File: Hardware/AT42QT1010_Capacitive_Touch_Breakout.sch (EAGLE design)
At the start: 28 parts, among them Q1 600mA/40V, U1 AT42QT1010 - UDFN

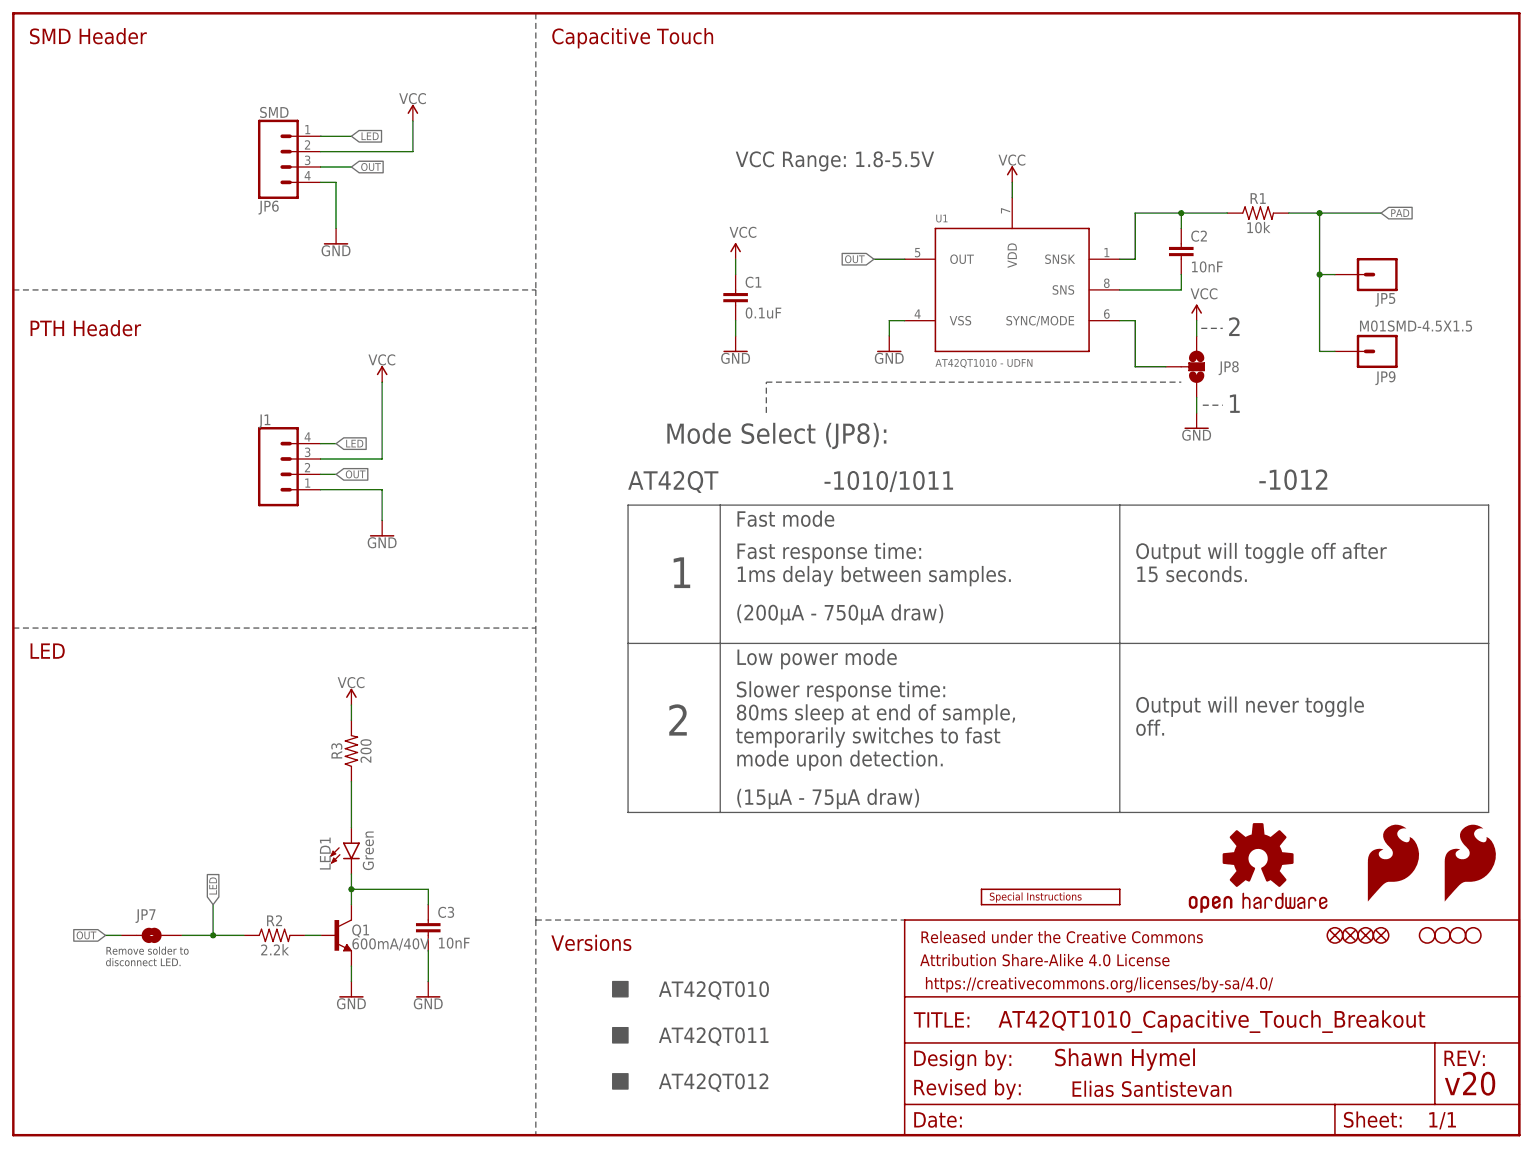
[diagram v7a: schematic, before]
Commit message: Update for REDS review
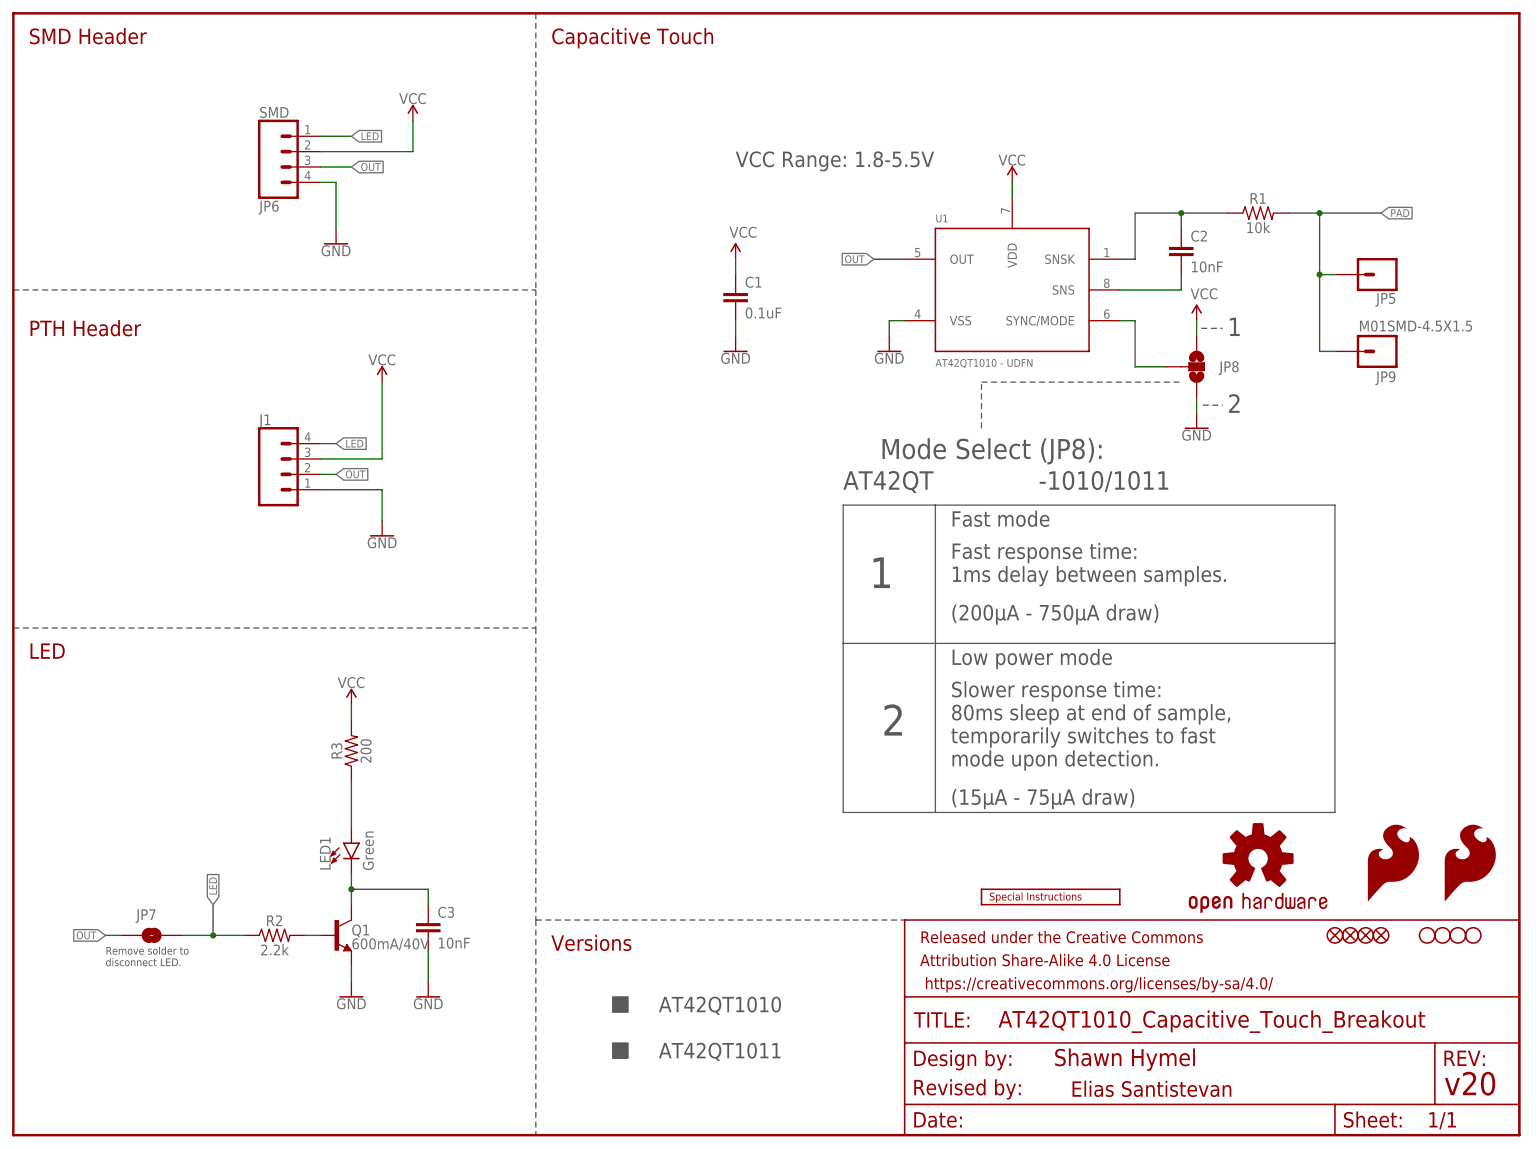
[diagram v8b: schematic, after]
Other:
- note added: "AT42QT1010"
- note added: "AT42QT1011"
- note removed: "-1012"
- note removed: "AT42QT010"
- note removed: "AT42QT011"
- note removed: "AT42QT012"
- note removed: "Output will never toggle off."
- note removed: "Output will toggle off after 15 seconds."
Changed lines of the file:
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@@
 <layer number="255" name="routoute" color="7" fill="1" visible="yes" active="yes"/>
 </layers>
-<schematic xreflabel="%F%N/%S" xrefpart="/%S.%C%R">
+<schematic xreflabel="%F%N/%S" xrefpart="1_/%S.%C%R">
 <attributes>
 </attributes>
@@
 <text x="2.54" y="132.08" size="2.54" layer="94" font="vector">PTH Header</text>
 <text x="2.54" y="78.74" size="2.54" layer="94" font="vector">LED</text>
-<text x="144.78" y="106.68" size="3.048" layer="97" font="vector" align="bottom-center">-1010/1011</text>
-<text x="119.38" y="100.584" size="2.54" layer="97" font="vector" ratio="15">Fast mode</text>
-<text x="119.38" y="91.44" size="2.54" layer="97" font="vector">Fast response time:
+<text x="180.34" y="106.68" size="3.048" layer="97" font="vector" align="bottom-center">-1010/1011</text>
+<text x="154.94" y="100.584" size="2.54" layer="97" font="vector" ratio="15">Fast mode</text>
+<text x="154.94" y="91.44" size="2.54" layer="97" font="vector">Fast response time:
 1ms delay between samples.</text>
-<text x="119.38" y="77.724" size="2.54" layer="97" font="vector" ratio="15">Low power mode</text>
-<text x="119.38" y="54.61" size="2.54" layer="97" font="vector">(15µA - 75µA draw)</text>
-<text x="119.38" y="60.96" size="2.54" layer="97" font="vector">Slower response time:
+<text x="154.94" y="77.724" size="2.54" layer="97" font="vector" ratio="15">Low power mode</text>
+<text x="154.94" y="54.61" size="2.54" layer="97" font="vector">(15µA - 75µA draw)</text>
+<text x="154.94" y="60.96" size="2.54" layer="97" font="vector">Slower response time:
 80ms sleep at end of sample,
 temporarily switches to fast
 mode upon detection.</text>
-<text x="119.38" y="85.09" size="2.54" layer="97" font="vector">(200µA - 750µA draw)</text>
-<wire x1="182.88" y1="104.14" x2="243.84" y2="104.14" width="0.1524" layer="97"/>
-<wire x1="243.84" y1="104.14" x2="243.84" y2="81.28" width="0.1524" layer="97"/>
-<wire x1="243.84" y1="81.28" x2="243.84" y2="53.34" width="0.1524" layer="97"/>
-<wire x1="243.84" y1="53.34" x2="182.88" y2="53.34" width="0.1524" layer="97"/>
+<text x="154.94" y="85.09" size="2.54" layer="97" font="vector">(200µA - 750µA draw)</text>
 <text x="148.59" y="6.604" size="2.54" layer="94" font="vector">Revised by:</text>
 <text x="174.752" y="6.35" size="2.54" layer="94" font="vector" ratio="10">Elias Santistevan</text>
@@
 <text x="15.24" y="27.94" size="1.27" layer="97" font="vector">Remove solder to
 disconnect LED.</text>
-<text x="126.238" y="114.3" size="3.302" layer="97" font="vector" ratio="10" align="bottom-center">Mode Select (JP8):</text>
-<wire x1="101.6" y1="104.14" x2="116.84" y2="104.14" width="0.1524" layer="97"/>
-<wire x1="116.84" y1="104.14" x2="182.88" y2="104.14" width="0.1524" layer="97"/>
-<wire x1="182.88" y1="104.14" x2="182.88" y2="81.28" width="0.1524" layer="97"/>
-<wire x1="182.88" y1="81.28" x2="182.88" y2="53.34" width="0.1524" layer="97"/>
-<wire x1="182.88" y1="53.34" x2="116.84" y2="53.34" width="0.1524" layer="97"/>
-<wire x1="116.84" y1="53.34" x2="101.6" y2="53.34" width="0.1524" layer="97"/>
-<wire x1="101.6" y1="53.34" x2="101.6" y2="81.28" width="0.1524" layer="97"/>
-<wire x1="101.6" y1="81.28" x2="101.6" y2="104.14" width="0.1524" layer="97"/>
-<wire x1="101.6" y1="81.28" x2="182.88" y2="81.28" width="0.1524" layer="97"/>
-<wire x1="116.84" y1="104.14" x2="116.84" y2="53.34" width="0.1524" layer="97"/>
-<text x="185.42" y="91.44" size="2.54" layer="97" font="vector">Output will toggle off after
-15 seconds.</text>
-<text x="185.42" y="66.04" size="2.54" layer="97" font="vector">Output will never toggle
-off.</text>
-<wire x1="182.88" y1="81.28" x2="243.84" y2="81.28" width="0.2032" layer="97"/>
-<text x="108.458" y="90.424" size="5.08" layer="97" font="vector" ratio="15">1</text>
-<text x="107.95" y="66.04" size="5.08" layer="97" font="vector" ratio="15">2</text>
-<text x="205.74" y="106.68" size="3.302" layer="97" font="vector">-1012</text>
-<wire x1="124.46" y1="119.38" x2="124.46" y2="124.46" width="0.2032" layer="97" style="shortdash"/>
-<wire x1="124.46" y1="124.46" x2="193.04" y2="124.46" width="0.2032" layer="97" style="shortdash"/>
-<text x="101.6" y="106.68" size="3.048" layer="97" font="vector">AT42QT </text>
+<text x="161.798" y="111.76" size="3.302" layer="97" font="vector" ratio="10" align="bottom-center">Mode Select (JP8):</text>
+<wire x1="137.16" y1="104.14" x2="152.4" y2="104.14" width="0.1524" layer="97"/>
+<wire x1="152.4" y1="104.14" x2="218.44" y2="104.14" width="0.1524" layer="97"/>
+<wire x1="218.44" y1="104.14" x2="218.44" y2="81.28" width="0.1524" layer="97"/>
+<wire x1="218.44" y1="81.28" x2="218.44" y2="53.34" width="0.1524" layer="97"/>
+<wire x1="218.44" y1="53.34" x2="152.4" y2="53.34" width="0.1524" layer="97"/>
+<wire x1="152.4" y1="53.34" x2="137.16" y2="53.34" width="0.1524" layer="97"/>
+<wire x1="137.16" y1="53.34" x2="137.16" y2="81.28" width="0.1524" layer="97"/>
+<wire x1="137.16" y1="81.28" x2="137.16" y2="104.14" width="0.1524" layer="97"/>
+<wire x1="137.16" y1="81.28" x2="218.44" y2="81.28" width="0.1524" layer="97"/>
+<wire x1="152.4" y1="104.14" x2="152.4" y2="53.34" width="0.1524" layer="97"/>
+<text x="141.478" y="90.424" size="5.08" layer="97" font="vector" ratio="15">1</text>
+<text x="143.51" y="66.04" size="5.08" layer="97" font="vector" ratio="15">2</text>
+<wire x1="160.02" y1="116.84" x2="160.02" y2="124.46" width="0.2032" layer="97" style="shortdash"/>
+<wire x1="160.02" y1="124.46" x2="193.04" y2="124.46" width="0.2032" layer="97" style="shortdash"/>
+<text x="137.16" y="106.68" size="3.048" layer="97" font="vector">AT42QT </text>
 <wire x1="86.36" y1="35.56" x2="147.32" y2="35.56" width="0.2032" layer="97" style="shortdash"/>
 <text x="88.9" y="30.48" size="2.54" layer="94" font="vector">Versions</text>
-<text x="106.68" y="22.86" size="2.54" layer="97" font="vector">AT42QT010</text>
-<text x="106.68" y="15.24" size="2.54" layer="97" font="vector">AT42QT011</text>
-<text x="106.68" y="7.62" size="2.54" layer="97" font="vector">AT42QT012</text>
+<text x="106.68" y="20.32" size="2.54" layer="97" font="vector">AT42QT1010</text>
+<text x="106.68" y="12.7" size="2.54" layer="97" font="vector">AT42QT1011</text>
 <polygon width="0.2032" layer="97">
-<vertex x="99.06" y="25.4"/>
 <vertex x="99.06" y="22.86"/>
+<vertex x="99.06" y="20.32"/>
+<vertex x="101.6" y="20.32"/>
 <vertex x="101.6" y="22.86"/>
-<vertex x="101.6" y="25.4"/>
 </polygon>
 <polygon width="0.2032" layer="97">
-<vertex x="99.06" y="17.78"/>
 <vertex x="99.06" y="15.24"/>
+<vertex x="99.06" y="12.7"/>
+<vertex x="101.6" y="12.7"/>
 <vertex x="101.6" y="15.24"/>
-<vertex x="101.6" y="17.78"/>
 </polygon>
-<polygon width="0.2032" layer="97">
-<vertex x="99.06" y="10.16"/>
-<vertex x="99.06" y="7.62"/>
-<vertex x="101.6" y="7.62"/>
-<vertex x="101.6" y="10.16"/>
-</polygon>
-<text x="200.66" y="119.38" size="3.048" layer="97" font="vector" ratio="15">1</text>
-<text x="200.66" y="132.08" size="3.048" layer="97" font="vector" ratio="15">2</text>
+<text x="200.66" y="132.08" size="3.048" layer="97" font="vector" ratio="15">1</text>
+<text x="200.66" y="119.38" size="3.048" layer="97" font="vector" ratio="15">2</text>
 <wire x1="196.596" y1="120.65" x2="199.898" y2="120.65" width="0.2032" layer="97" style="shortdash"/>
 <wire x1="196.342" y1="133.35" x2="199.898" y2="133.35" width="0.2032" layer="97" style="shortdash"/>
